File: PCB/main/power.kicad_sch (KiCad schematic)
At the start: 22 parts, among them J5 47346-0001, Q1 IRF9540NPbF, U1 MCP73831-2-OT, U2 FT232RL, U3 MCP1700-3302E_TO92

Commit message: added test points and jumpers
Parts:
- removed JP1: Jumper_3_Open, Jumper:SolderJumper-3_P1.3mm_Open_Pad1.0x1.5mm_NumberLabels, symbol EEE3088_PROJECT-rescue:Jumper_3_Open-Jumper
- added J6, J7: PZ254V-11-02P, SamacSys_Parts:HDRV2W64P0X254_1X2_508X250X873P, symbol SamacSys_Parts_power:PZ254V-11-02P
- added J8: MTP125-1103S1, SamacSys_Parts:HDRV3W64P0X254_1X3_762X250X885P, symbol SamacSys_Parts_power:MTP125-1103S1
- added TP1, TP2, TP3, TP4: 5017, SamacSys_Parts:5017, symbol SamacSys_Parts_power:5017
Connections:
- net +5V: now also TP3.1
- net USART1_TX: now also J6.2; no longer U2.1 (TXD)
- net USATR1_RX: now also J7.1; no longer U2.5 (RXD)
- net VCC: now also J8.2
- net Vsupply: now also TP4.1
- net at BT1.1 (+), C4.2, Q1.2 (S)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: now also TP1.1
- net at C7.1, U3.2 (VI): now also J8.1, TP2.1; no longer D3.1 (K)
- net at D3.2 (A): now also Q1.1 (D)
- net at D2.1 (K): now also D3.1 (K), J8.3; no longer Q1.1 (D)
- new net: J6.1, U2.1 (TXD)
- new net: J7.2, U2.5 (RXD)
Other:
- moved on the sheet: C7, C8, D2, D3, U3

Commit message: gerber files and dat
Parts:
- renumbered D3 to D2, D2 to D3, TP3 to TP1, TP1 to TP2, TP2 to TP3
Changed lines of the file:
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@@
   (symbol (lib_id "Device:D_Schottky") (at 199.39 101.6 0) (mirror y) (unit 1)
     (in_bom yes) (on_board yes)
-    (property "Reference" "D3" (id 0) (at 199.39 96.1136 0))
+    (property "Reference" "D2" (id 0) (at 199.39 96.1136 0))
     (property "Value" "BAT60J" (id 1) (at 199.39 99.06 0))
     (property "Footprint" "Diode_SMD:D_SOD-323" (id 2) (at 199.39 101.6 0)
@@
   (symbol (lib_id "Diode:BAT60A") (at 205.74 83.82 90) (unit 1)
     (in_bom yes) (on_board yes)
-    (property "Reference" "D2" (id 0) (at 207.7466 82.6516 90)
+    (property "Reference" "D3" (id 0) (at 207.7466 82.6516 90)
       (effects (font (size 1.27 1.27)) (justify right))
     )
@@
   (symbol (lib_id "power:PWR_FLAG") (at 158.75 144.78 180) (unit 1)
     (in_bom yes) (on_board yes) (fields_autoplaced)
-    (property "Reference" "#FLG04" (id 0) (at 158.75 146.685 0)
+    (property "Reference" "#FLG05" (id 0) (at 158.75 146.685 0)
       (effects (font (size 1.27 1.27)) hide)
     )
@@
   (symbol (lib_id "SamacSys_Parts_power:5017") (at 121.92 68.58 90) (unit 1)
     (in_bom yes) (on_board yes)
-    (property "Reference" "TP3" (id 0) (at 115.57 52.07 90)
+    (property "Reference" "TP1" (id 0) (at 115.57 52.07 90)
       (effects (font (size 1.27 1.27)) (justify right))
     )
@@
   (symbol (lib_id "power:GND") (at 110.49 93.98 0) (unit 1)
     (in_bom yes) (on_board yes) (fields_autoplaced)
-    (property "Reference" "#PWR0111" (id 0) (at 110.49 100.33 0)
+    (property "Reference" "#PWR018" (id 0) (at 110.49 100.33 0)
       (effects (font (size 1.27 1.27)) hide)
     )
@@
   (symbol (lib_id "power:GND") (at 111.76 102.87 0) (unit 1)
     (in_bom yes) (on_board yes) (fields_autoplaced)
-    (property "Reference" "#PWR0109" (id 0) (at 111.76 109.22 0)
+    (property "Reference" "#PWR019" (id 0) (at 111.76 109.22 0)
       (effects (font (size 1.27 1.27)) hide)
     )
@@
   (symbol (lib_id "power:PWR_FLAG") (at 125.73 64.77 270) (unit 1)
     (in_bom yes) (on_board yes) (fields_autoplaced)
-    (property "Reference" "#FLG01" (id 0) (at 127.635 64.77 0)
+    (property "Reference" "#FLG03" (id 0) (at 127.635 64.77 0)
       (effects (font (size 1.27 1.27)) hide)
     )
@@
   (symbol (lib_id "power:GND") (at 175.26 190.5 0) (unit 1)
     (in_bom yes) (on_board yes) (fields_autoplaced)
-    (property "Reference" "#PWR0105" (id 0) (at 175.26 196.85 0)
+    (property "Reference" "#PWR024" (id 0) (at 175.26 196.85 0)
       (effects (font (size 1.27 1.27)) hide)
     )
@@
   (symbol (lib_id "power:PWR_FLAG") (at 237.49 101.6 0) (unit 1)
     (in_bom yes) (on_board yes) (fields_autoplaced)
-    (property "Reference" "#FLG05" (id 0) (at 237.49 99.695 0)
+    (property "Reference" "#FLG06" (id 0) (at 237.49 99.695 0)
       (effects (font (size 1.27 1.27)) hide)
     )
@@
   (symbol (lib_id "power:GND") (at 246.38 91.44 180) (unit 1)
     (in_bom yes) (on_board yes) (fields_autoplaced)
-    (property "Reference" "#PWR0108" (id 0) (at 246.38 85.09 0)
+    (property "Reference" "#PWR027" (id 0) (at 246.38 85.09 0)
       (effects (font (size 1.27 1.27)) hide)
     )
@@
   (symbol (lib_id "power:PWR_FLAG") (at 143.51 129.54 0) (unit 1)
     (in_bom yes) (on_board yes) (fields_autoplaced)
-    (property "Reference" "#FLG03" (id 0) (at 143.51 127.635 0)
+    (property "Reference" "#FLG04" (id 0) (at 143.51 127.635 0)
       (effects (font (size 1.27 1.27)) hide)
     )
@@
   (symbol (lib_id "SamacSys_Parts_power:5017") (at 181.61 101.6 90) (unit 1)
     (in_bom yes) (on_board yes)
-    (property "Reference" "TP1" (id 0) (at 181.61 82.55 90)
+    (property "Reference" "TP2" (id 0) (at 181.61 82.55 90)
       (effects (font (size 1.27 1.27)) (justify right))
     )
@@
   (symbol (lib_id "power:GND") (at 236.22 124.46 0) (unit 1)
     (in_bom yes) (on_board yes) (fields_autoplaced)
-    (property "Reference" "#PWR0107" (id 0) (at 236.22 130.81 0)
+    (property "Reference" "#PWR026" (id 0) (at 236.22 130.81 0)
       (effects (font (size 1.27 1.27)) hide)
     )
@@
   (symbol (lib_id "power:GND") (at 119.38 102.87 0) (unit 1)
     (in_bom yes) (on_board yes) (fields_autoplaced)
-    (property "Reference" "#PWR0110" (id 0) (at 119.38 109.22 0)
+    (property "Reference" "#PWR020" (id 0) (at 119.38 109.22 0)
       (effects (font (size 1.27 1.27)) hide)
     )
@@
   (symbol (lib_id "power:GND") (at 104.14 142.24 270) (unit 1)
     (in_bom yes) (on_board yes)
-    (property "Reference" "#PWR0106" (id 0) (at 97.79 142.24 0)
+    (property "Reference" "#PWR017" (id 0) (at 97.79 142.24 0)
       (effects (font (size 1.27 1.27)) hide)
     )
@@
   (symbol (lib_id "power:GND") (at 134.62 123.19 0) (unit 1)
     (in_bom yes) (on_board yes) (fields_autoplaced)
-    (property "Reference" "#PWR0101" (id 0) (at 134.62 129.54 0)
+    (property "Reference" "#PWR022" (id 0) (at 134.62 129.54 0)
       (effects (font (size 1.27 1.27)) hide)
     )
@@
   (symbol (lib_id "SamacSys_Parts_power:5017") (at 222.25 101.6 90) (unit 1)
     (in_bom yes) (on_board yes)
-    (property "Reference" "TP2" (id 0) (at 220.98 81.28 90)
+    (property "Reference" "TP3" (id 0) (at 220.98 81.28 90)
       (effects (font (size 1.27 1.27)) (justify right))
     )
@@
   (symbol (lib_id "power:GND") (at 176.53 91.44 0) (unit 1)
     (in_bom yes) (on_board yes)
-    (property "Reference" "#PWR0102" (id 0) (at 176.53 97.79 0)
+    (property "Reference" "#PWR025" (id 0) (at 176.53 97.79 0)
       (effects (font (size 1.27 1.27)) hide)
     )
@@
   (symbol (lib_id "power:GND") (at 170.18 81.28 90) (unit 1)
     (in_bom yes) (on_board yes) (fields_autoplaced)
-    (property "Reference" "#PWR0103" (id 0) (at 176.53 81.28 0)
-      (effects (font (size 1.27 1.27)) hide)
-    )
+    (property "Reference" "#PWR023" (id 0) (at 176.53 81.28 0)
+      (effects (font (size 1.27 1.27)) hide)
+    )

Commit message: created BOM
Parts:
- BT1: Comment (none) -> battery holder; Price($) (none) -> 0
- C1: Comment (none) -> 10nF; JLCPCB Part Number (none) -> C15195; LCSC (none) -> C15195; Price($) (none) -> 0.0011
- C2, C5: Comment (none) -> 100nF; JLCPCB Part Number (none) -> C14663; LCSC (none) -> C14663; Price($) (none) -> 0.0025
- C3, C4, C6: Comment (none) -> 4,7uF; JLCPCB Part Number (none) -> C69335; LCSC (none) -> C69335; Price($) (none) -> 0.0186
- C7, C8: Comment (none) -> 1uF; JLCPCB Part Number (none) -> C15849; LCSC (none) -> C15849; Price($) (none) -> 0.0055
- D1: Comment (none) -> LED; JLCPCB Part Number (none) -> C264544; LCSC (none) -> C264544; Price($) (none) -> 0.1512
- D2, D3: Comment (none) -> BAT60J; JLCPCB Part Number (none) -> C133103; LCSC (none) -> C133103; Price($) (none) -> 0.273
- FB1: Comment (none) -> Ferrite_Bead; JLCPCB Part Number (none) -> C1002; LCSC (none) -> C1002; Price($) (none) -> 0,0052
- J5: Comment (none) -> USB_B_Micro; JLCPCB Part Number (none) -> C132560; LCSC (none) -> C132560; Price($) (none) -> 0.3515
- J6, J7: Comment (none) -> 2 pin male header; JLCPCB Part Number (none) -> C492401; LCSC (none) -> C492401; Price($) (none) -> 0.0106
- J8: Comment (none) -> 3 pin male header; JLCPCB Part Number (none) -> C358685; LCSC (none) -> C358685; Price($) (none) -> 0.0172
- Q1: Comment (none) -> transistor; JLCPCB Part Number (none) -> C2575; LCSC (none) -> C2575; Price($) (none) -> 0.6714
- R1: Comment (none) -> 2k; JLCPCB Part Number (none) -> C433871; LCSC (none) -> C433871; Price($) (none) -> 0.0109
- R2: Comment (none) -> 470R; JLCPCB Part Number (none) -> C114564; LCSC (none) -> C114564; Price($) (none) -> 0.0026
- R3: Comment (none) -> 10k; JLCPCB Part Number (none) -> C25804; LCSC (none) -> C25804; Price($) (none) -> 0.0012
- TP1, TP2, TP3, TP4: Comment (none) -> test point; JLCPCB Part Number (none) -> C238130; LCSC (none) -> C238130; Price($) (none) -> 0.4796
- U1: Comment (none) -> BATTERY MANAGEMENT IC; JLCPCB Part Number (none) -> C424093; LCSC (none) -> C424093; Price($) (none) -> 1.1526
- U2: Comment (none) -> FTDI; JLCPCB Part Number (none) -> C8690; LCSC (none) -> C8690; Price($) (none) -> 6.3298
- U3: Comment (none) -> LDO; JLCPCB Part Number (none) -> C39051; LCSC (none) -> C39051; Price($) (none) -> 1.1889

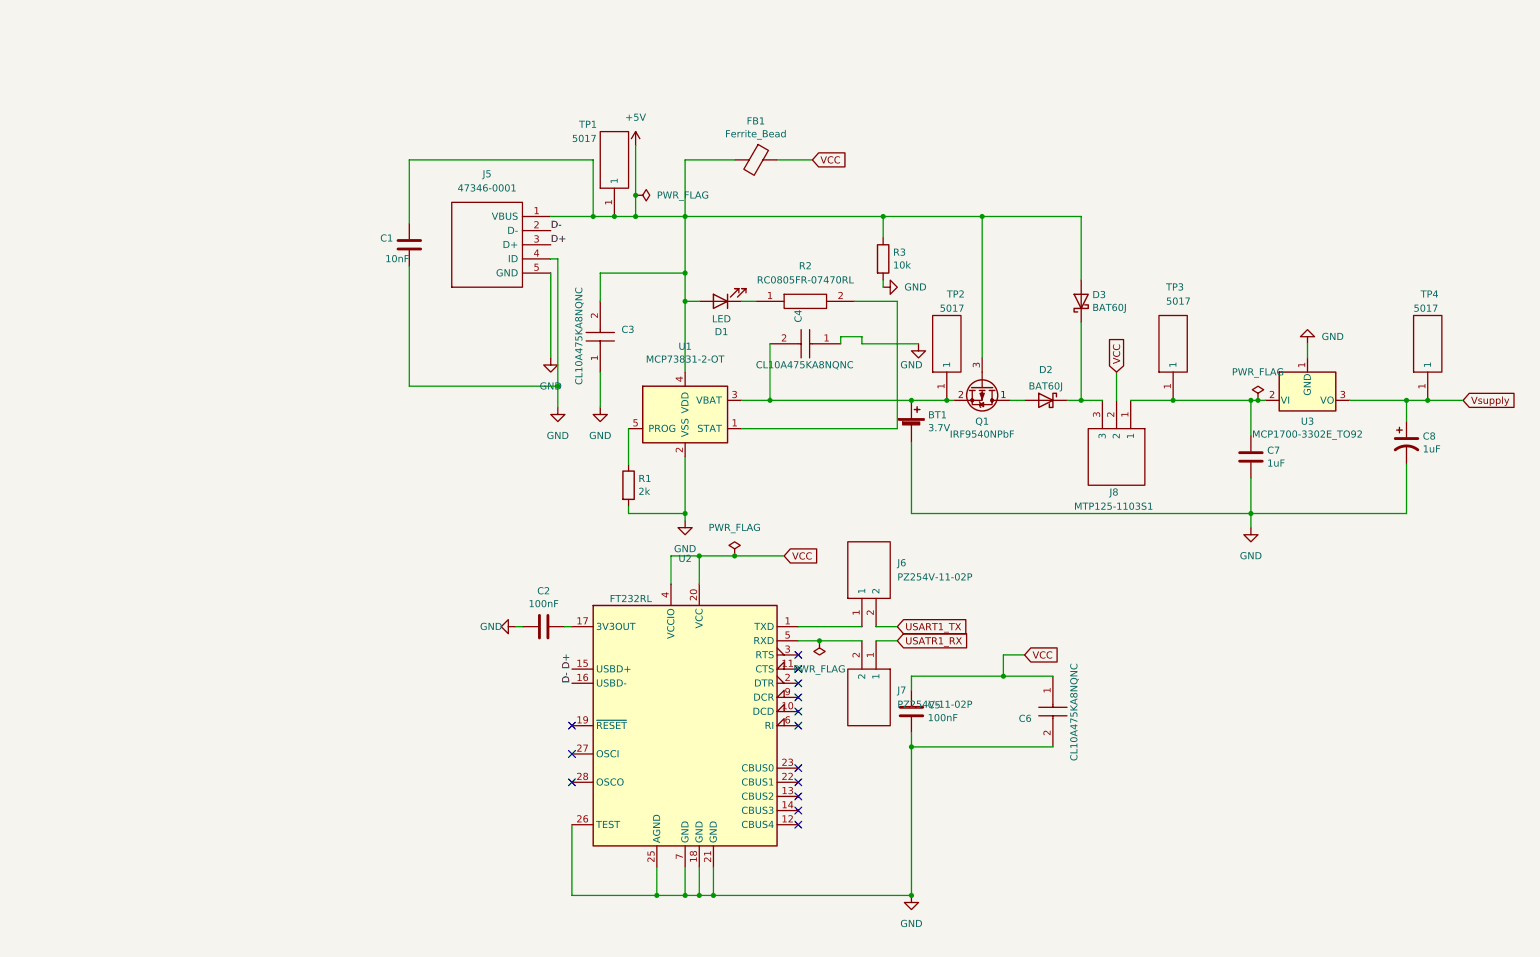
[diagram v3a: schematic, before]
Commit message: modified power schematic
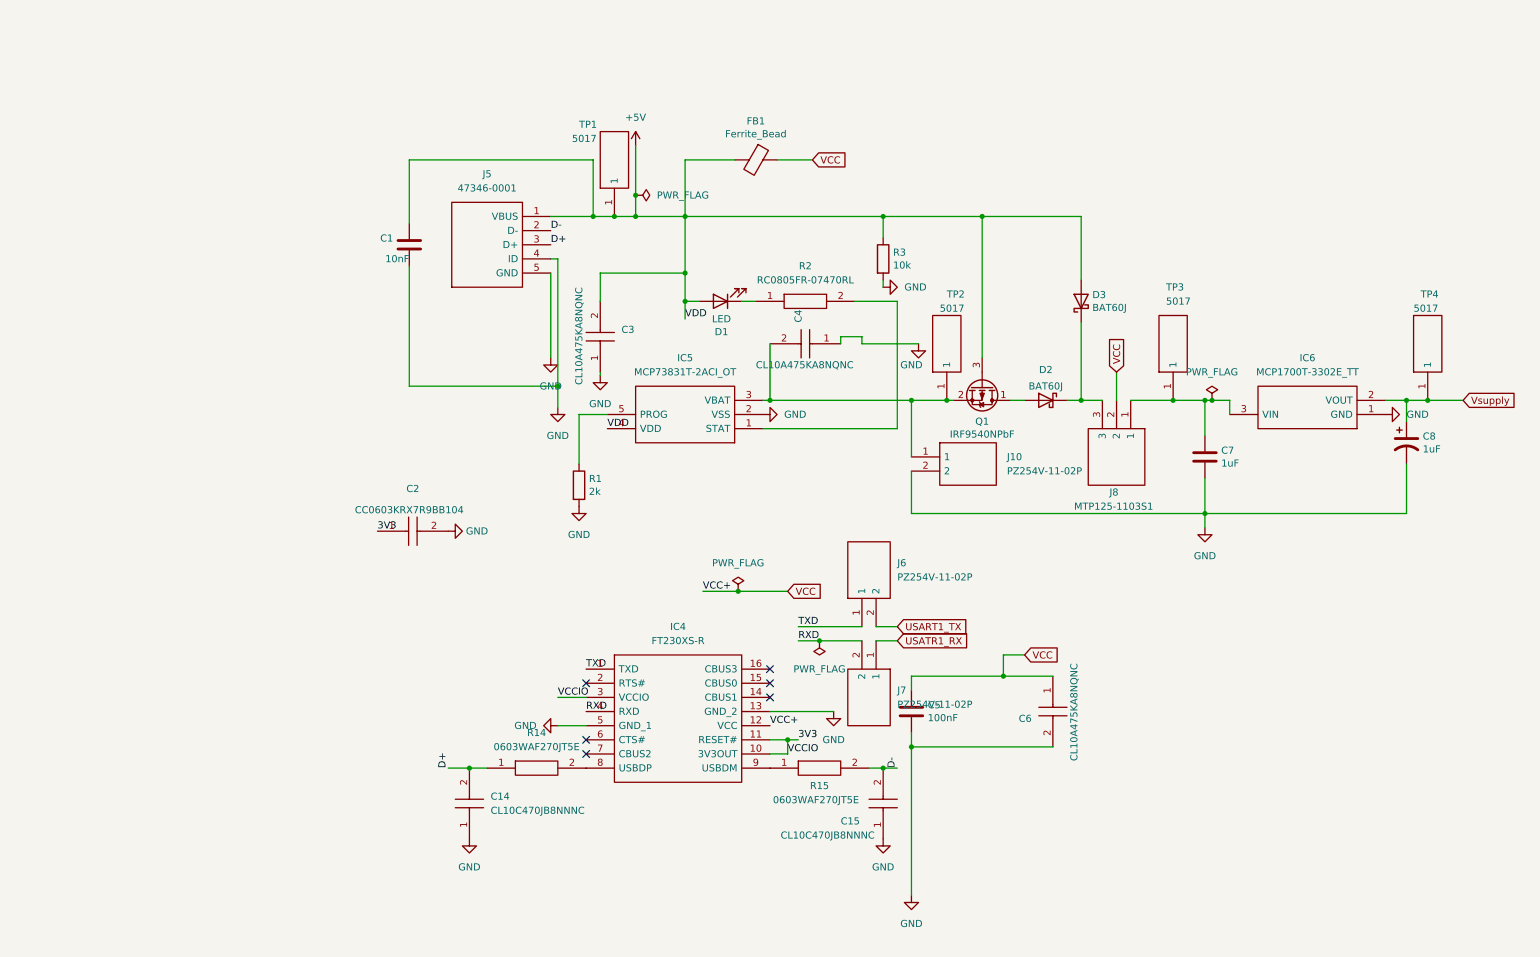
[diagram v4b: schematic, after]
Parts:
- removed BT1: 3.7V, Battery:BatteryHolder_Keystone_1042_1x18650, symbol Device:Battery_Cell
- removed C2: 100nF, SamacSys_Parts:CAPC1608X90N, symbol Device:C
- removed U1: MCP73831-2-OT, Package_TO_SOT_SMD:SOT-23-5, symbol Battery_Management:MCP73831-2-OT
- removed U2: FT232RL, Package_SO:SSOP-28_5.3x10.2mm_P0.65mm, symbol Interface_USB:FT232RL
- removed U3: MCP1700-3302E_TO92, Package_TO_SOT_THT:TO-92_Inline, symbol Regulator_Linear:MCP1700-3302E_TO92
- added C14, C15: CL10C470JB8NNNC, CAPC1608X90N, symbol SamacSys_Parts_power:CL10C470JB8NNNC
- added C2: CC0603KRX7R9BB104, CAPC1608X90N, symbol SamacSys_Parts_power:CC0603KRX7R9BB104
- added IC4: FT230XS-R, SOP64P599X175-16N, symbol SamacSys_Parts_power:FT230XS-R
- added IC5: MCP73831T-2ACI_OT, SOT95P270X145-5N, symbol SamacSys_Parts_power:MCP73831T-2ACI_OT
- added IC6: MCP1700T-3302E_TT, SOT95P237X112-3N, symbol SamacSys_Parts_power:MCP1700T-3302E_TT
- added J10: PZ254V-11-02P, HDRV2W64P0X254_1X2_508X250X873P, symbol SamacSys_Parts_power:PZ254V-11-02P
- added R14, R15: 0603WAF270JT5E, RESC1608X55N, symbol SamacSys_Parts_power:0603WAF270JT5E
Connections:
- net +5V: now also IC5.4 (VDD)
- net D+: now also C14.2, R14.1
- net D-: now also C15.2, R15.2
- net GND: now also C14.1, C15.1, C2.2, IC4.13 (GND_2), IC4.5 (GND_1), IC5.2 (VSS), IC6.1 (GND), J10.2
- net VCC: now also IC4.12 (VCC)
- net Vsupply: now also IC6.2 (VOUT)
- net at R2.2: now also IC5.1 (STAT)
- net at C4.2, Q1.2 (S), TP2.1: now also IC5.3 (VBAT), J10.1
- net at R1.1: now also IC5.5 (PROG)
- net at C7.1, J8.1, TP3.1: now also IC6.3 (VIN)
- net TXD: now reaches J6.1
- net TXD: now also IC4.1 (TXD)
- net RXD: now reaches J7.2
- net RXD: now also IC4.4 (RXD)
- new net: IC4.9 (USBDM), R15.1
- new net: IC4.8 (USBDP), R14.2
- new net 3V3: C2.1, IC4.10 (3V3OUT), IC4.11 (RESET#), IC4.3 (VCCIO)
- no-connect marks 14 -> 6
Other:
- moved on the sheet: C7, R1
